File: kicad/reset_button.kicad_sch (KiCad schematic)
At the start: 2 parts, among them SW1 PTS526_SM15_SMTR2_LFS

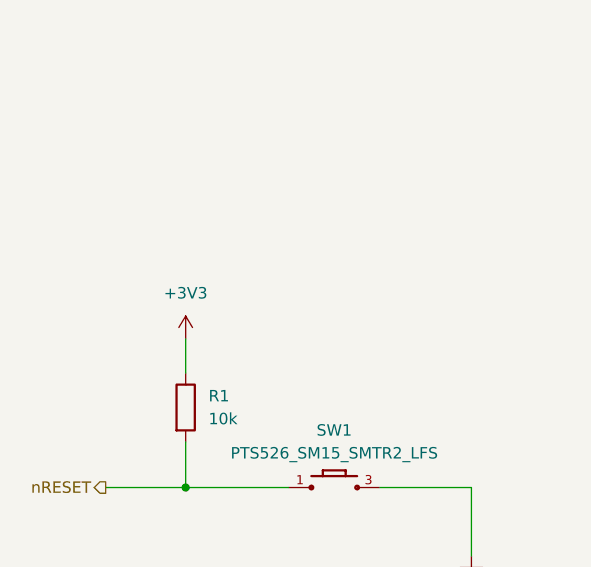
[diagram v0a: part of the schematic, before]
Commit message: feat: remake power management and use the same as the reference DK
Signed-off-by: Bobo Bäck Engström <bobo@id8-engineering.io>
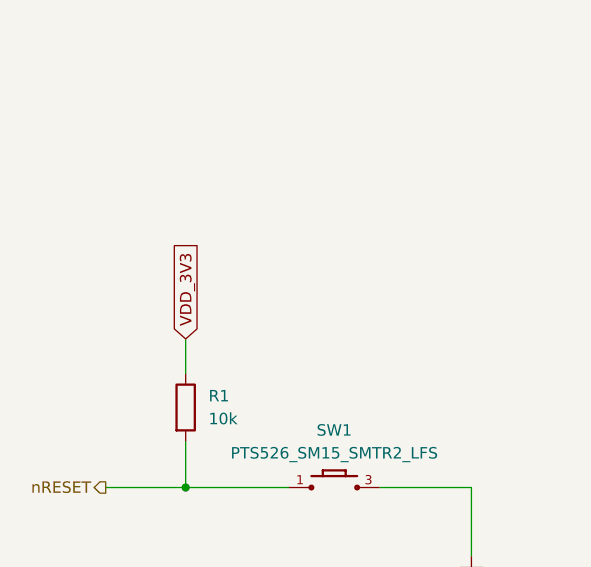
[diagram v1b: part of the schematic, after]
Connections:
- net +3V3 renamed VDD_3V3
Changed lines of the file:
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@@
+		)
+	)
+	(global_label "VDD_3V3"
+		(shape input)
+		(at 69.85 76.2 90)
+		(fields_autoplaced yes)
+		(effects
+			(font
+				(size 1.27 1.27)
+			)
+			(justify left)
+		)
+		(property "Intersheetrefs" "${INTERSHEET_REFS}"
+			(at 69.85 65.111 90)
+			(effects
+				(font
+					(size 1.27 1.27)
+				)
+				(justify left)
+				(hide yes)
+			)
 		)
 	)
@@
 					(unit 1)
 				)
-			)
-		)
-	)
-	(symbol
-		(lib_id "seven_lib:+3V3")
-		(at 69.85 76.2 0)
-		(unit 1)
-		(exclude_from_sim no)
-		(in_bom yes)
-		(on_board yes)
-		(dnp no)
-		(fields_autoplaced yes)
-		(property "Reference" "#PWR07"
-			(at 69.85 80.01 0)
-			(effects
-				(font
-					(size 1.27 1.27)
-				)
-				(hide yes)
-			)
-		)
-		(property "Value" "+3V3"
-			(at 69.85 71.12 0)
-			(effects
-				(font
-					(size 1.27 1.27)
-				)
-			)
-		)
-		(property "Footprint" ""
-			(at 69.85 76.2 0)
-			(effects
-				(font
-					(size 1.27 1.27)
-				)
-				(hide yes)
-			)
-		)
-		(property "Datasheet" ""
-			(at 69.85 76.2 0)
-			(effects
-				(font
-					(size 1.27 1.27)
-				)
-				(hide yes)
-			)
-		)
-		(property "Description" "Power symbol creates a global label with name \"+3V3\""
-			(at 69.85 76.2 0)
-			(effects
-				(font
-					(size 1.27 1.27)
-				)
-				(hide yes)
-			)
-		)
-		(pin "1"
-		)
-		(instances
-			(project ""
-				(path "/8e3cc843-5797-49f3-8b3a-1c11450ccd1e/fcef6494-c0b2-4cc5-a2e1-aeb845f0853f"
-					(reference "#PWR07")
-					(unit 1)
-				)

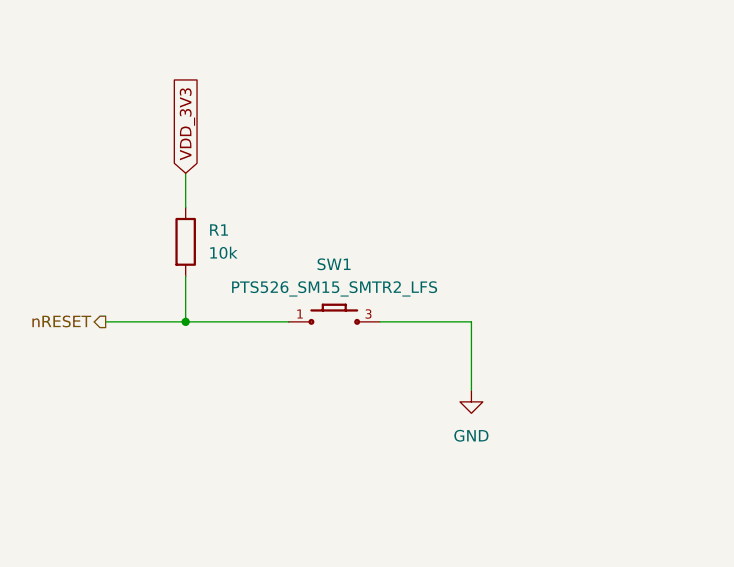
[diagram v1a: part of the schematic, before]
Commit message: feat: swap reset button to TL3336AF160Q
Signed-off-by: Bobo Bäck Engström <bobo@id8-engineering.io>
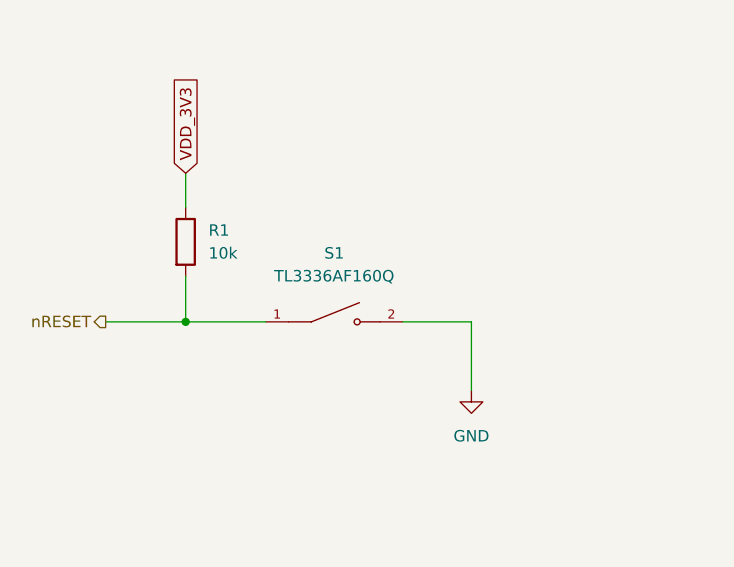
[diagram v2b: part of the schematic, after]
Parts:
- removed SW1: PTS526_SM15_SMTR2_LFS, seven-lib:PTS526SM15SMTR2LFS, symbol seven_lib:PTS526_SM15_SMTR2_LFS
- added S1: TL3336AF160Q, seven-lib:SW_TL3336AF160Q, symbol seven_lib:TL3336AF160Q
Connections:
- net GND: now also S1.2
- net nRESET: now also S1.1
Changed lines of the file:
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@@
-	(wire
-		(pts
-			(xy 81.28 92.71) (xy 69.85 92.71)
-		)
-		(stroke
-			(width 0)
-			(type default)
-		)
-	)
 	(wire
 		(pts
@@
 	(wire
 		(pts
-			(xy 91.44 92.71) (xy 101.6 92.71)
-		)
-		(stroke
-			(width 0)
-			(type default)
-		)
-	)
-	(wire
-		(pts
 			(xy 69.85 87.63) (xy 69.85 92.71)
 		)
@@
 		)
 	)
+	(wire
+		(pts
+			(xy 78.74 92.71) (xy 69.85 92.71)
+		)
+		(stroke
+			(width 0)
+			(type default)
+		)
+	)
 	(polyline
 		(pts
@@
 			(width 0)
 			(type dash)
+		)
+	)
+	(wire
+		(pts
+			(xy 93.98 92.71) (xy 101.6 92.71)
+		)
+		(stroke
+			(width 0)
+			(type default)
 		)
 	)
@@
 	)
 	(symbol
-		(lib_id "seven_lib:PTS526_SM15_SMTR2_LFS")
+		(lib_id "seven_lib:TL3336AF160Q")
 		(at 86.36 92.71 0)
 		(unit 1)
@@
 		(dnp no)
 		(fields_autoplaced yes)
-		(property "Reference" "SW1"
-			(at 86.36 86.36 0)
-			(effects
-				(font
-					(size 1.27 1.27)
-				)
-			)
-		)
-		(property "Value" "PTS526_SM15_SMTR2_LFS"
-			(at 86.36 88.9 0)
-			(effects
-				(font
-					(size 1.27 1.27)
-				)
-			)
-		)
-		(property "Footprint" "seven-lib:PTS526SM15SMTR2LFS"
-			(at 86.36 92.71 0)
-			(effects
-				(font
-					(size 1.27 1.27)
-				)
-				(justify bottom)
-				(hide yes)
-			)
-		)
-		(property "Datasheet" "https://www.ckswitches.com/media/2780/pts526.pdf"
-			(at 86.36 92.71 0)
-			(effects
-				(font
-					(size 1.27 1.27)
-				)
-				(hide yes)
-			)
-		)
-		(property "Description" "Tactile Switches 50mA 12VDC, 5.2x5.2mm, 1.5mm H, 160gf, G leads, No ground pin, metal actuator"
-			(at 86.36 92.71 0)
-			(effects
-				(font
-					(size 1.27 1.27)
-				)
-				(justify bottom)
-				(hide yes)
-			)
-		)
-		(property "MANUFACTURER_NAME" "C & K COMPONENTS"
-			(at 86.36 92.71 0)
-			(effects
-				(font
-					(size 1.27 1.27)
-				)
-				(justify bottom)
-				(hide yes)
-			)
-		)
-		(property "MF" "C&K"
-			(at 86.36 92.71 0)
-			(effects
-				(font
-					(size 1.27 1.27)
-				)
-				(justify bottom)
-				(hide yes)
-			)
-		)
-		(property "MOUSER_PRICE-STOCK" "https://www.mouser.co.uk/ProductDetail/CK/PTS526-SM15-SMTR2-LFS?qs=UXgszm6BlbENivbslIA%252B5g%3D%3D"
-			(at 86.36 92.71 0)
-			(effects
-				(font
-					(size 1.27 1.27)
-				)
-				(justify bottom)
-				(hide yes)
-			)
-		)
-		(property "MOUSER_PART_NUMBER" "611-PTS526SM15SMTR2L"
+		(property "Reference" "S1"
+			(at 86.36 85.09 0)
+			(effects
+				(font
+					(size 1.27 1.27)
+				)
+			)
+		)
+		(property "Value" "TL3336AF160Q"
+			(at 86.36 87.63 0)
+			(effects
+				(font
+					(size 1.27 1.27)
+				)
+			)
+		)
+		(property "Footprint" "seven-lib:SW_TL3336AF160Q"
+			(at 86.36 92.71 0)
+			(effects
+				(font
+					(size 1.27 1.27)
+				)
+				(justify bottom)
+				(hide yes)
+			)
+		)
+		(property "Datasheet" ""
+			(at 86.36 92.71 0)
+			(effects
+				(font
+					(size 1.27 1.27)
+				)
+				(hide yes)
+			)
+		)
+		(property "Description" ""
+			(at 86.36 92.71 0)
+			(effects
+				(font
+					(size 1.27 1.27)
+				)
+				(hide yes)
+			)
+		)
+		(property "MF" "E-Switch"
+			(at 86.36 92.71 0)
+			(effects
+				(font
+					(size 1.27 1.27)
+				)
+				(justify bottom)
+				(hide yes)
+			)
+		)
+		(property "MAXIMUM_PACKAGE_HEIGHT" "7.1mm"
+			(at 86.36 92.71 0)
+			(effects
+				(font
+					(size 1.27 1.27)
+				)
+				(justify bottom)
+				(hide yes)
+			)
+		)
+		(property "Package" "None"
 			(at 86.36 92.71 0)
 			(effects
@@
 			)
 		)
-		(property "Package" "None"
-			(at 86.36 92.71 0)
-			(effects
-				(font
-					(size 1.27 1.27)
-				)
-				(justify bottom)
-				(hide yes)
-			)
-		)
-		(property "Check_prices" "https://www.snapeda.com/parts/PTS526%20SM15%20SMTR2%20LFS/C%2526K/view-part/?ref=eda"
-			(at 86.36 92.71 0)
-			(effects
-				(font
-					(size 1.27 1.27)
-				)
-				(justify bottom)
-				(hide yes)
-			)
-		)
-		(property "HEIGHT" "1.5mm"
-			(at 86.36 92.71 0)
-			(effects
-				(font
-					(size 1.27 1.27)
-				)
-				(justify bottom)
-				(hide yes)
-			)
-		)
-		(property "MP" "PTS526 SM15 SMTR2 LFS"
-			(at 86.36 92.71 0)
-			(effects
-				(font
-					(size 1.27 1.27)
-				)
-				(justify bottom)
-				(hide yes)
-			)
-		)
-		(property "SnapEDA_Link" "https://www.snapeda.com/parts/PTS526%20SM15%20SMTR2%20LFS/C%2526K/view-part/?ref=snap"
-			(at 86.36 92.71 0)
-			(effects
-				(font
-					(size 1.27 1.27)
-				)
-				(justify bottom)
-				(hide yes)
-			)
-		)
-		(property "ARROW_PRICE-STOCK" "https://www.arrow.com/en/products/pts526-sm15-smtr2-lfs/ck"
-			(at 86.36 92.71 0)
-			(effects
-				(font
-					(size 1.27 1.27)
-				)
-				(justify bottom)
-				(hide yes)
-			)
-		)
-		(property "ARROW_PART_NUMBER" "PTS526 SM15 SMTR2 LFS"
-			(at 86.36 92.71 0)
-			(effects
-				(font
-					(size 1.27 1.27)
-				)
-				(justify bottom)
-				(hide yes)
-			)
-		)
-		(property "Description_1" "Tactile Switch SPST-NO Top Actuated Surface Mount"
+		(property "Check_prices" "https://www.snapeda.com/parts/TL3336AF160Q/E-Switch/view-part/?ref=eda"
+			(at 86.36 92.71 0)
+			(effects
+				(font
+					(size 1.27 1.27)
+				)
+				(justify bottom)
+				(hide yes)
+			)
+		)
+		(property "STANDARD" "Manufacturer Recommendations"
+			(at 86.36 92.71 0)
+			(effects
+				(font
+					(size 1.27 1.27)
+				)
+				(justify bottom)
+				(hide yes)
+			)
+		)
+		(property "PARTREV" "3.30.2021"
+			(at 86.36 92.71 0)
+			(effects
+				(font
+					(size 1.27 1.27)
+				)
+				(justify bottom)
+				(hide yes)
+			)
+		)
+		(property "SnapEDA_Link" "https://www.snapeda.com/parts/TL3336AF160Q/E-Switch/view-part/?ref=snap"
+			(at 86.36 92.71 0)
+			(effects
+				(font
+					(size 1.27 1.27)
+				)
+				(justify bottom)
+				(hide yes)
+			)
+		)
+		(property "MP" "TL3336AF160Q"
+			(at 86.36 92.71 0)
+			(effects
+				(font
+					(size 1.27 1.27)
+				)
+				(justify bottom)
+				(hide yes)
+			)
+		)
+		(property "Purchase-URL" "https://www.snapeda.com/api/url_track_click_mouser/?unipart_id=5907806&manufacturer=E-Switch&part_name=TL3336AF160Q&search_term=None"
+			(at 86.36 92.71 0)
+			(effects
+				(font
+					(size 1.27 1.27)
+				)
+				(justify bottom)
+				(hide yes)
+			)
+		)
+		(property "Description_1" "Tactile Switch, SPST-NO, OFF-(ON), Top Actuated, R/A, 0.05A, 12V, TL3336A Series | E-Switch TL3336AF160Q"
+			(at 86.36 92.71 0)
+			(effects
+				(font
+					(size 1.27 1.27)
+				)
+				(justify bottom)
+				(hide yes)
+			)
+		)
+		(property "MANUFACTURER" "E-Switch"
 			(at 86.36 92.71 0)
 			(effects
@@
 			)
 		)
-		(property "MANUFACTURER_PART_NUMBER" "PTS526 SM15 SMTR2 LFS"
-			(at 86.36 92.71 0)
-			(effects
-				(font
-					(size 1.27 1.27)
-				)
-				(justify bottom)
-				(hide yes)
-			)
-		)
-		(pin "4"
+		(property "SNAPEDA_PN" "TL3336AF160Q"
+			(at 86.36 92.71 0)
+			(effects
+				(font
+					(size 1.27 1.27)
+				)
+				(justify bottom)
+				(hide yes)
+			)
 		)
 		(pin "2"
-		)
-		(pin "3"
 		)
 		(pin "1"
@@
 			(project ""
 				(path "/8e3cc843-5797-49f3-8b3a-1c11450ccd1e/fcef6494-c0b2-4cc5-a2e1-aeb845f0853f"
-					(reference "SW1")
+					(reference "S1")
 					(unit 1)
 				)

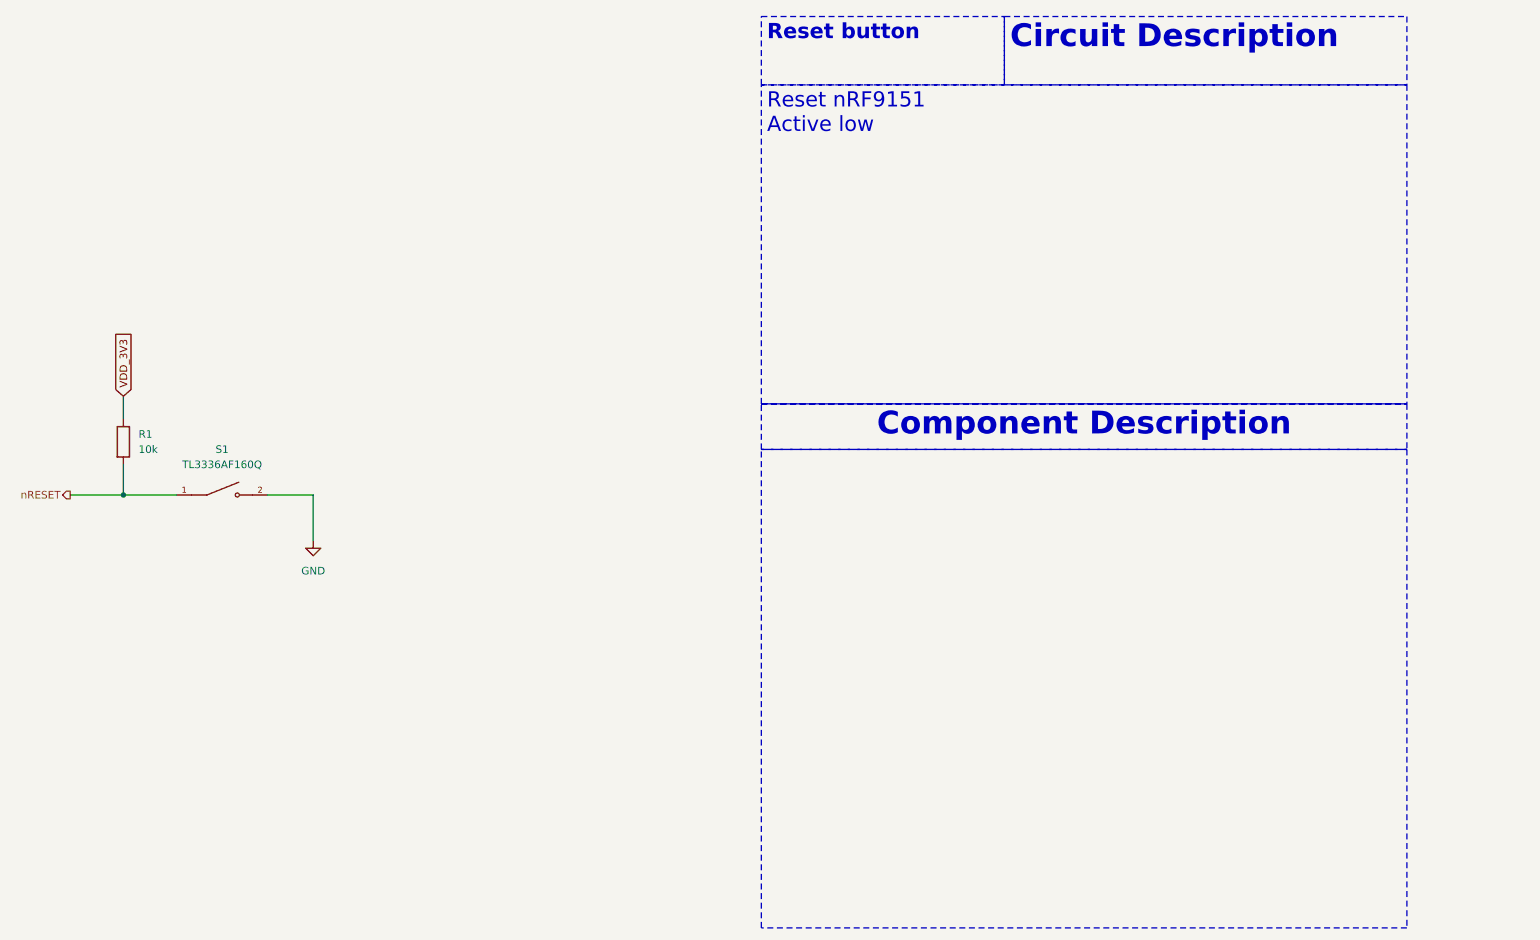
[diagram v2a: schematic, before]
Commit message: docs: update documentation to be more accurate
Signed-off-by: Bobo Bäck Engström <bobo@id8-engineering.io>
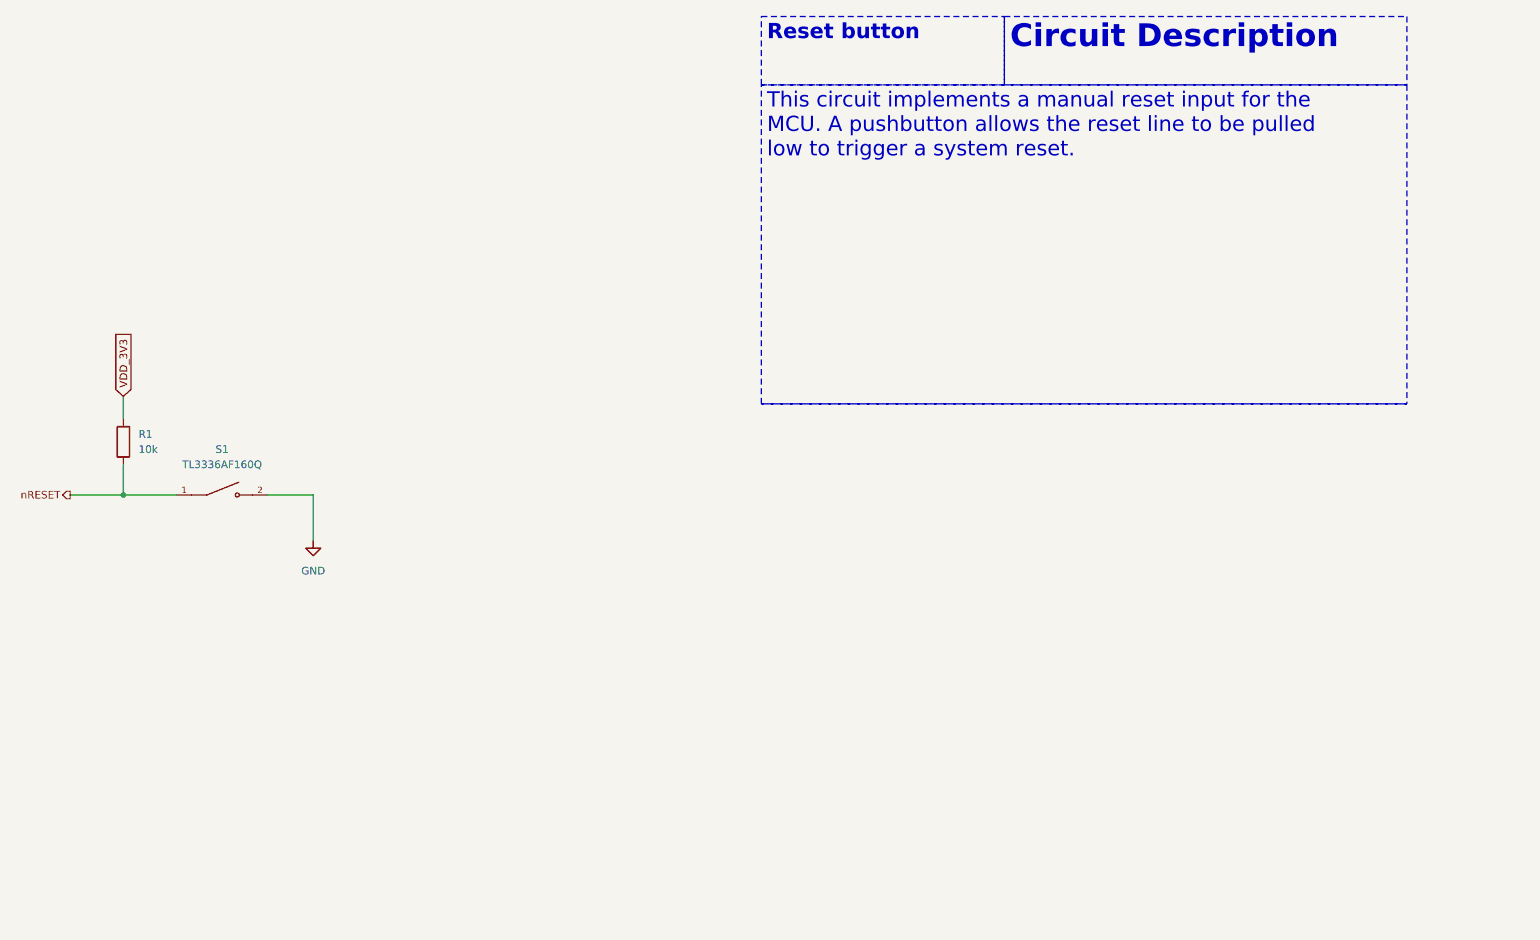
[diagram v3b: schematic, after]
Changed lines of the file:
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@@
-		)
-	)
-	(text_box "Component Description\n"
-		(exclude_from_sim no)
-		(at 176.53 77.47 0)
-		(size 107.95 7.62)
-		(margins 0.9525 0.9525 0.9525 0.9525)
-		(stroke
-			(width 0)
-			(type dash)
-		)
-		(fill
-			(type none)
-		)
-		(effects
-			(font
-				(size 3.81 3.81)
-				(thickness 0.762)
-				(bold yes)
-			)
-			(justify top)
 		)
 	)
@@
 		)
 	)
-	(text_box "\n"
-		(exclude_from_sim no)
-		(at 176.53 85.09 0)
-		(size 107.95 80.01)
-		(margins 0.9525 0.9525 0.9525 0.9525)
-		(stroke
-			(width 0)
-			(type dash)
-		)
-		(fill
-			(type none)
-		)
-		(effects
-			(font
-				(size 2.54 2.54)
-			)
-			(justify left top)
-		)
-	)
-	(text_box "Reset nRF9151\nActive low"
+	(text_box "This circuit implements a manual reset input for the MCU. A pushbutton allows the reset line to be pulled low to trigger a system reset."
 		(exclude_from_sim no)
 		(at 176.53 24.13 0)
@@
 			)
 		)
-		(property "Datasheet" ""
+		(property "Datasheet" "https://www.mouser.se/datasheet/3/315/1/TL3336AF160Q.pdf"
 			(at 86.36 92.71 0)
 			(effects

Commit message: fix: change R fp to a smaller one
Signed-off-by: Bobo Bäck Engström <bobo@id8-engineering.io>
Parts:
- R1: footprint seven-lib:R_0603_1608Metric -> seven-lib:R_0402_1005Metric
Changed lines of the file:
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@@
 			)
 		)
-		(property "Footprint" "seven-lib:R_0603_1608Metric"
+		(property "Footprint" "seven-lib:R_0402_1005Metric"
 			(at 68.072 83.82 90)
 			(effects

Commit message: fix: changes made according to review meeting
Signed-off-by: Bobo Bäck Engström <bobo@id8-engineering.io>
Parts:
- added TP11: RESET_BUTTON, seven-lib:TestPoint_Pad_2.0x2.0mm, symbol seven_lib:TestPoint
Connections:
- net nRESET: now also TP11.1
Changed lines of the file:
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@@
+	)
+	(junction
+		(at 66.04 92.71)
+		(diameter 0)
+		(color 0 0 0 0)
 	)
 	(junction
@@
 	(wire
 		(pts
-			(xy 60.96 92.71) (xy 69.85 92.71)
+			(xy 66.04 99.06) (xy 66.04 92.71)
+		)
+		(stroke
+			(width 0)
+			(type default)
+		)
+	)
+	(wire
+		(pts
+			(xy 66.04 92.71) (xy 69.85 92.71)
+		)
+		(stroke
+			(width 0)
+			(type default)
+		)
+	)
+	(wire
+		(pts
+			(xy 60.96 92.71) (xy 66.04 92.71)
 		)
 		(stroke
@@
 					(unit 1)
 				)
+			)
+		)
+	)
+	(symbol
+		(lib_id "seven_lib:TestPoint")
+		(at 66.04 99.06 180)
+		(unit 1)
+		(exclude_from_sim no)
+		(in_bom yes)
+		(on_board yes)
+		(dnp no)
+		(property "Reference" "TP11"
+			(at 62.103 100.965 0)
+			(effects
+				(font
+					(size 1.27 1.27)
+				)
+			)
+		)
+		(property "Value" "RESET_BUTTON"
+			(at 62.103 103.505 0)
+			(effects
+				(font
+					(size 1.27 1.27)
+				)
+			)
+		)
+		(property "Footprint" "seven-lib:TestPoint_Pad_2.0x2.0mm"
+			(at 60.96 99.06 0)
+			(effects
+				(font
+					(size 1.27 1.27)
+				)
+				(hide yes)
+			)
+		)
+		(property "Datasheet" "~"
+			(at 60.96 99.06 0)
+			(effects
+				(font
+					(size 1.27 1.27)
+				)
+				(hide yes)
+			)
+		)
+		(property "Description" "test point"
+			(at 66.04 99.06 0)
+			(effects
+				(font
+					(size 1.27 1.27)
+				)
+				(hide yes)
+			)
+		)
+		(pin "1"
+		)
+		(instances
+			(project "seven"
+				(path "/8e3cc843-5797-49f3-8b3a-1c11450ccd1e/fcef6494-c0b2-4cc5-a2e1-aeb845f0853f"
+					(reference "TP11")
+					(unit 1)
+				)

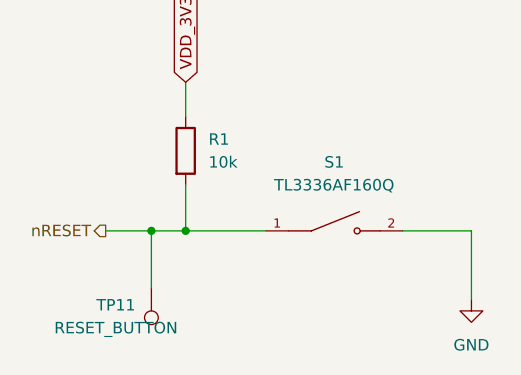
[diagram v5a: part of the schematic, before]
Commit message: feat(PCB): set component-placement example on PCB
This pr will fail due to DRC, skip this and lets have a conversation
about the placement only

Signed-off-by: Bobo Bäck Engström <bobo@id8-engineering.io>
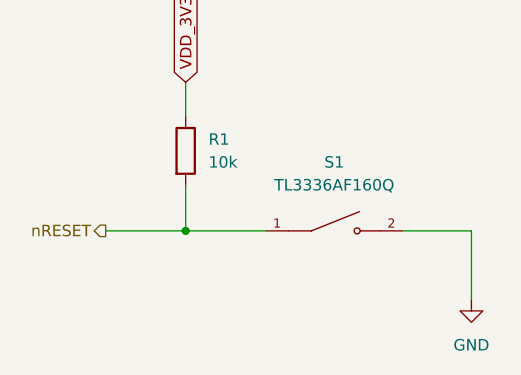
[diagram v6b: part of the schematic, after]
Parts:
- removed TP11: RESET_BUTTON, seven-lib:TestPoint_Pad_2.0x2.0mm, symbol seven_lib:TestPoint
- R1: MPN (none) -> RC0402FR-0710KL
- S1: MPN (none) -> TL3336AF160Q
